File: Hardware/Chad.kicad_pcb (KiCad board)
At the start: 4 copper layers, 99 parts, among them J1 RBUS, J3 ServoCH1, J4 ServoCH2, J5 USB_C_Receptacle_USB2.0, U1 ESP32-S3, U2 SN65HVD230, U3 LM66200DRLR, U4 MAX77827AEFD+T, U5 SC4215, U6 SiC437BED-T1-GE3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

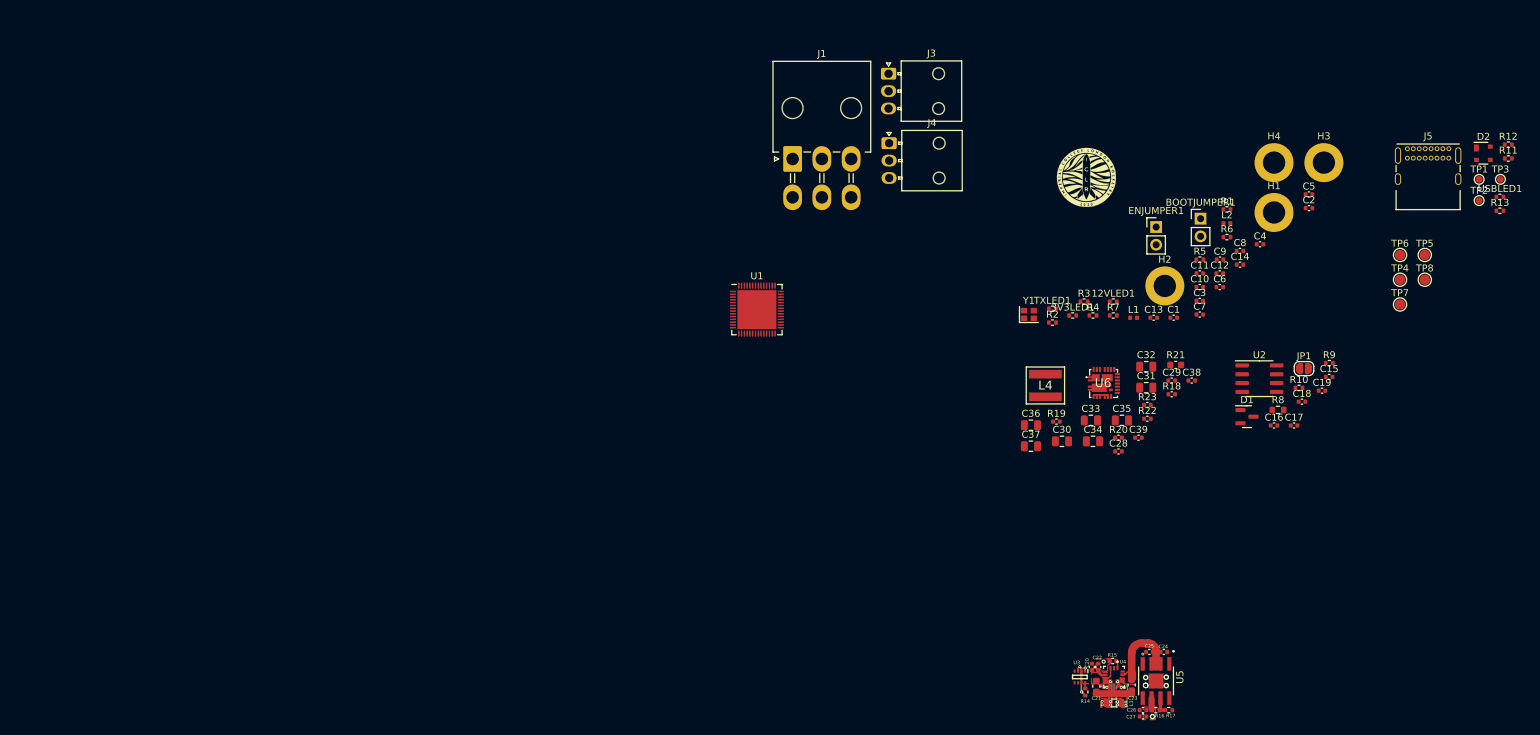
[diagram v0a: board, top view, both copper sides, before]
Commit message: initial layout for rough sizing
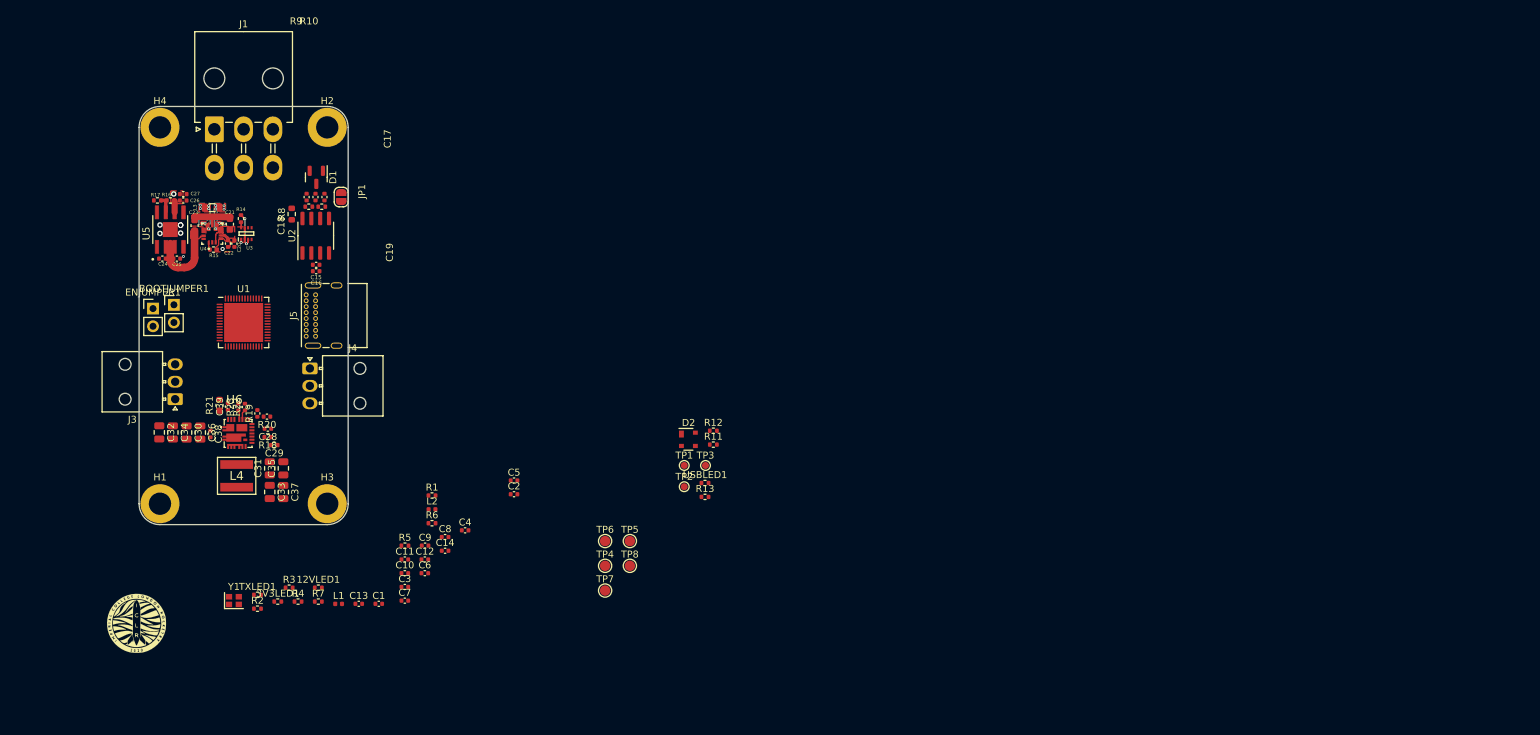
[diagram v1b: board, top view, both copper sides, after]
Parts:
- moved H1 165.2 mm to (35.0, 99.1)
- moved R17 162.5 mm to (34.6, 55.6), turned to 180 degrees
- moved J5 160.3 mm to (56.0, 75.1), turned to 90 degrees
- moved H4 159.9 mm to (35.0, 45.1)
- moved R16 159.2 mm to (36.5, 55.6), turned to 180 degrees
- moved C27 156.8 mm to (38.3, 54.7), turned to 180 degrees
- moved C26 155.9 mm to (38.3, 55.6), turned to 180 degrees
- moved U5 155.6 mm to (36.5, 59.8), turned to 90 degrees
- moved C24 154.4 mm to (35.3, 63.9), turned to 180 degrees
- moved H3 151.1 mm to (59.0, 99.1)
- moved LOGO1 150.6 mm to (31.6, 116.2)
- moved C25 150.5 mm to (37.4, 63.9), turned to 0 degrees
- moved C23 149.8 mm to (40.0, 59.2), turned to 90 degrees
- moved R9 148.1 mm to (56.4, 56.5)
- moved BOOTJUMPER1 147.8 mm to (37.0, 70.5)
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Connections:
- net Net-(C39-Pad1) renamed /buckC/BOOT
- net Net-(R21-Pad1) renamed /buckC/PHASE
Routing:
- net Net-(R22-Pad1): track 0.00 -> 1.45 mm
- net Net-(R23-Pad1): track 0.00 -> 1.36 mm
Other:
- board outline added: 30 x 60 mm

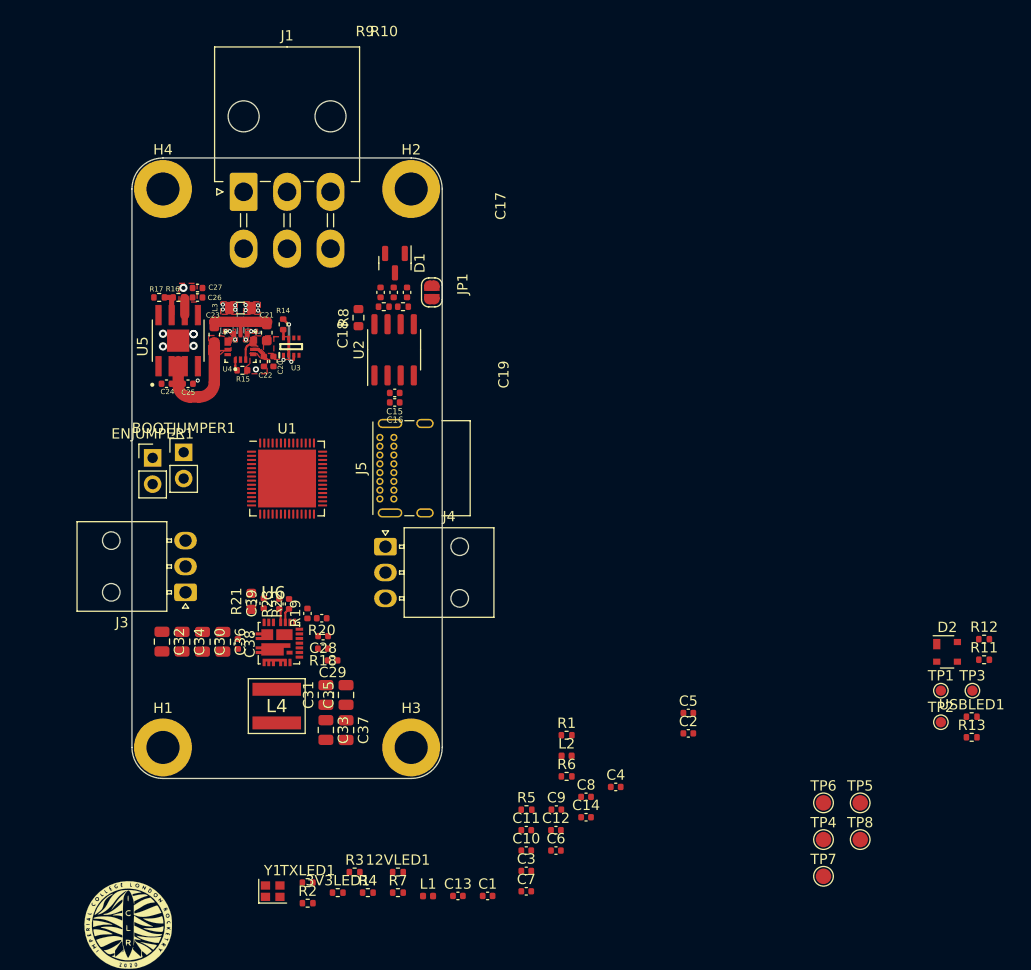
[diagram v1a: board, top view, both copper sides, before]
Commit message: Mostly completed RBUS side, still buck converter side to do
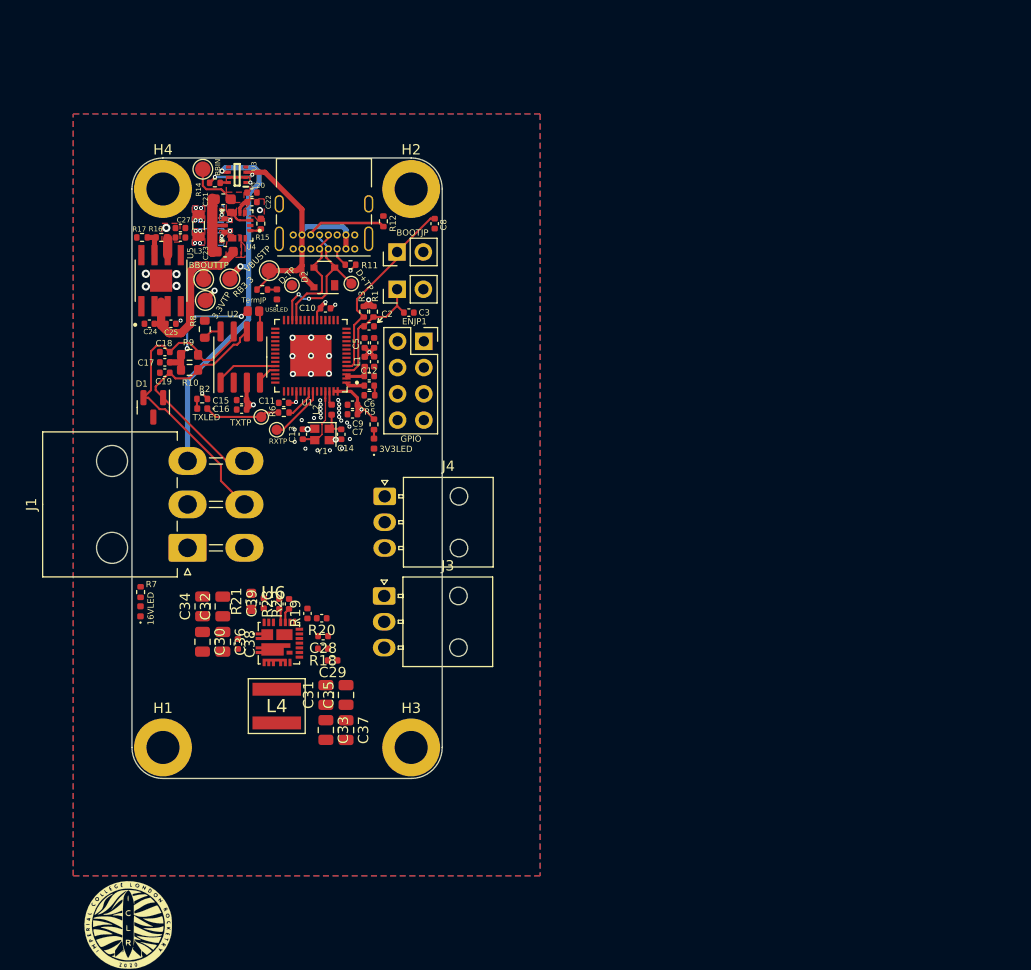
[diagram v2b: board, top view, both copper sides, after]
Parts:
- removed TP3: TestPoint, TestPoint:TestPoint_Pad_D1.0mm
- added J2: GPIO Breakout, Connector_PinSocket_2.54mm:PinSocket_2x04_P2.54mm_Vertical, F.Cu at (60.2, 59.8)
- added TP10: TestPoint, TestPoint:TestPoint_Pad_D1.0mm, F.Cu at (46.0, 68.4)
- added TP9: TestPoint, TestPoint:TestPoint_Pad_D1.0mm, F.Cu at (44.5, 67.1)
- 12VLED1, TXLED1, USBLED1: footprint Resistor_SMD:R_0402_1005Metric -> LED_SMD:LED_0402_1005Metric
- C17: value 0.1uF -> 47nF
- JP1: footprint Jumper:SolderJumper-2_P1.3mm_Open_RoundedPad1.0x1.5mm -> iclr:SmallerSolderJP
- R10, R9: footprint Resistor_SMD:R_0402_1005Metric -> Resistor_SMD:R_0603_1608Metric
- U1: footprint Package_DFN_QFN:QFN-56-1EP_7x7mm_P0.4mm_EP5.6x5.6mm -> iclr:QFN40P700X700X90-57N
- e: renamed from 3V3LED1; footprint Resistor_SMD:R_0402_1005Metric -> LED_SMD:LED_0402_1005Metric
- moved TP4 88.3 mm to (38.9, 43.2)
- moved TP8 83.4 mm to (38.9, 53.8)
- moved R13 81.1 mm to (44.6, 54.8)
- moved TP7 79.4 mm to (45.3, 53.0)
- moved TP5 79.3 mm to (41.5, 53.8)
- moved USBLED1 78.6 mm to (46.0, 55.3), turned to 90 degrees
- moved TP6 77.0 mm to (39.1, 55.9)
- moved TP1 74.0 mm to (47.5, 54.4)
- moved R11 72.2 mm to (53.1, 52.4)
- moved TP2 71.1 mm to (53.2, 54.2)
- moved R12 70.8 mm to (56.3, 48.2), turned to -90 degrees
- moved D2 70.3 mm to (50.6, 53.6), turned to 180 degrees
- moved C8 57.3 mm to (61.3, 48.4), turned to -90 degrees
- moved C10 55.9 mm to (50.7, 56.6)
- moved C3 55.2 mm to (58.8, 57.0)
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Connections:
- D2 pad 2: VBUS -> /Data+
- D2 pad 4: /Data+ -> VBUS
- U1 pad 38: unconnected-(U1-Pad38) -> /CAN_TX
- U1 pad 39: unconnected-(U1-Pad39) -> /CAN_RX
- U1 pad 50: unconnected-(U1-Pad50) -> /RXD
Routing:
- net RBUS_uC_V: track 0.00 -> 37.8 mm, vias 0 -> 2
- net /CAN+: track 0.00 -> 32.1 mm
- net VBUS: track 5.27 -> 33.4 mm
- net /CAN-: track 0.00 -> 23.4 mm
- net +3V3: track 1.61 -> 23.6 mm, vias 1 -> 9
- net /BOOT: track 0.00 -> 19.1 mm
- net /Data+: track 0.00 -> 15.1 mm, vias 0 -> 2
- net Net-(C17-Pad1): track 0.00 -> 12.5 mm, vias 0 -> 2
- net /CHIP_PU: track 0.00 -> 12.1 mm
- net /Data-: track 0.00 -> 11.1 mm
- net Net-(J5-PadB5): track 0.00 -> 7.74 mm
- net /TXD: track 0.00 -> 7.40 mm
- net Net-(C13-Pad1): track 0.00 -> 6.72 mm
- net /Power/BBOUT: track 12.3 -> 18.6 mm
- net /CAN_TX: track 0.00 -> 6.16 mm
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- added copper zone on In2.Cu, net +3V3
- added copper zone on B.Cu, net GND
- added copper zone on In1.Cu, net GND

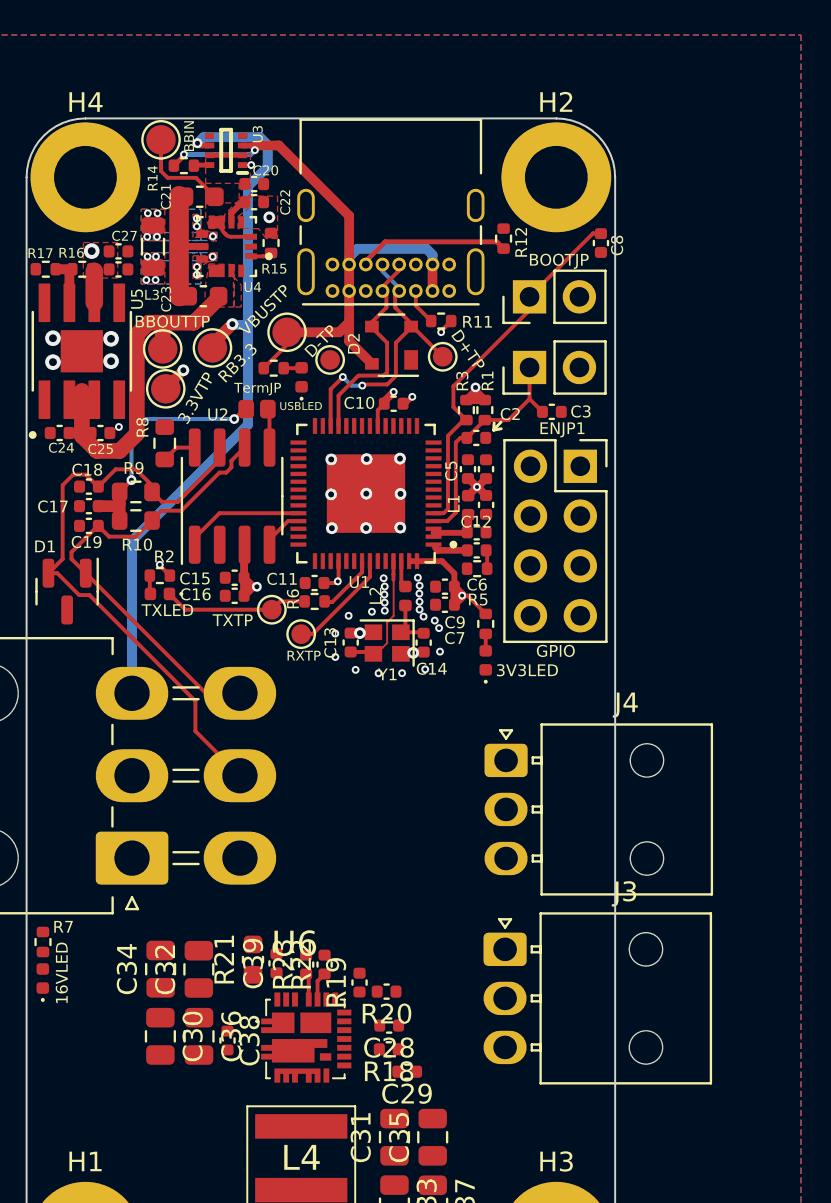
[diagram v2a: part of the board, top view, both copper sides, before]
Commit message: new USB port, added 3d models for the taller connectors
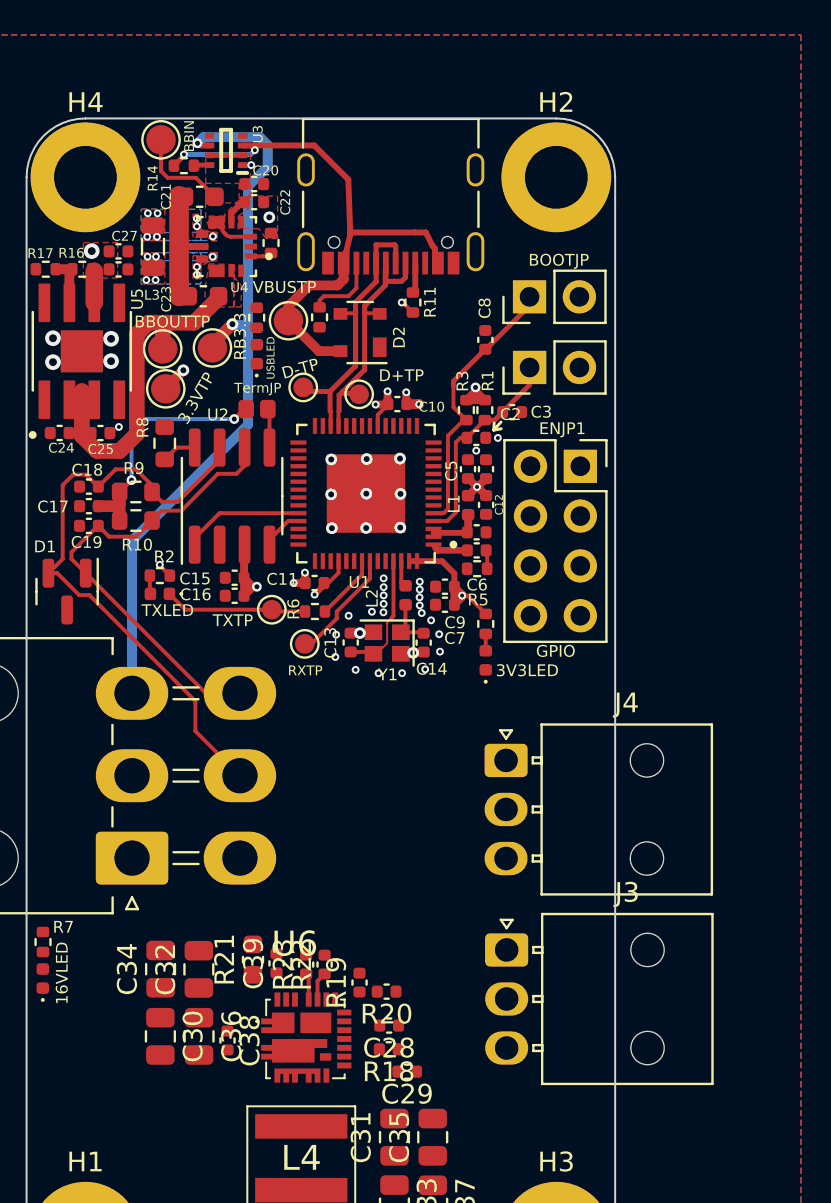
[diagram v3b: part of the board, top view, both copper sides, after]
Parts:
- J3: value ServoCH1 -> ServoCH2
- J5: footprint Connector_USB:USB_C_Receptacle_GCT_USB4085 -> Connector_USB:USB_C_Receptacle_Palconn_UTC16-G
- moved R12 10.2 mm to (46.9, 52.2), turned to 90 degrees
- moved C8 7.69 mm to (55.4, 53.4), turned to 90 degrees
- moved J5 4.93 mm to (50.6, 47.0)
- moved TP1 4.67 mm to (49.0, 56.1)
- moved R13 2.72 mm to (43.7, 52.2), turned to -90 degrees
- moved USBLED1 2.57 mm to (43.7, 54.1)
- moved C3 2.03 mm to (56.7, 57.1)
- moved TP2 1.96 mm to (46.1, 55.8)
- moved D2 1.73 mm to (49.0, 53.0)
- moved R11 1.72 mm to (51.7, 51.5), turned to -90 degrees
- moved TP7 0.59 mm to (45.4, 52.4)
- moved TP10 0.53 mm to (46.2, 68.9)
- moved R6 0.51 mm to (46.7, 67.2)
- moved C10 0.19 mm to (50.9, 56.6)
- moved J3 0.09 mm to (56.5, 84.5)
- renumbered e to 3V3LED1, TP2 to TP1, TP1 to TP2
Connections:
- D2 pad 2: /Data+ -> /Data-
- D2 pad 3: /Data- -> /Data+
- J3 pad 1: GND -> (no net)
- J3 pad 2: +6V -> (no net)
- J3 pad 3: /Servo1PWM -> (no net)
- TP1 pad 1: /Data+ -> /Data-
- TP2 pad 1: /Data- -> /Data+
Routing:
- net /BOOT: track 19.1 -> 15.1 mm
- net Net-(J5-PadB5): track 7.74 -> 3.76 mm
- net VBUS: track 33.4 -> 29.5 mm
- net /Data-: track 11.1 -> 13.7 mm
- net GND: track 8.12 -> 9.95 mm, vias 42 -> 46
- net /CHIP_PU: track 12.1 -> 10.8 mm
- net /CAN+: track 32.1 -> 31.0 mm
- net +3V3: track 23.6 -> 24.7 mm, vias 9 -> 10
- net /Data+: track 15.1 -> 14.1 mm, vias 2 -> 0
- net Net-(R13-Pad2): track 0.92 -> 0.00 mm
